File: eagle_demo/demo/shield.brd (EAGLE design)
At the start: 70 x 50 mm, 13 parts, among them X301 MALE_2X1-T-VERTICAL, X302 MALE_2X10-T-VERTICAL_2.54MM

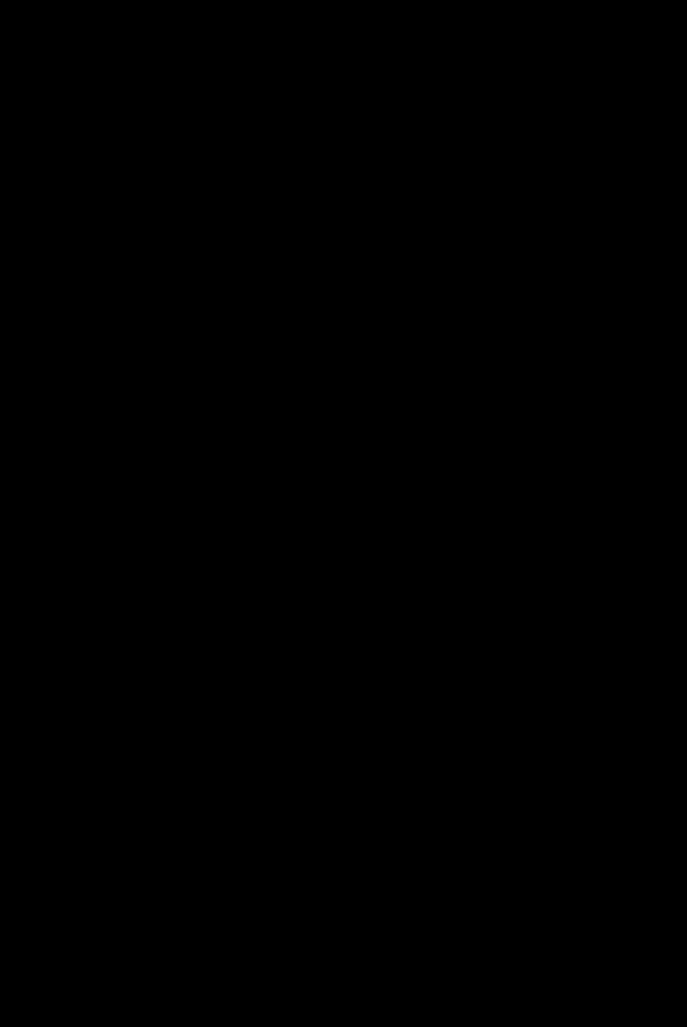
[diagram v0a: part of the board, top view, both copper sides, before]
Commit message: step 1.3 shield schematic updated
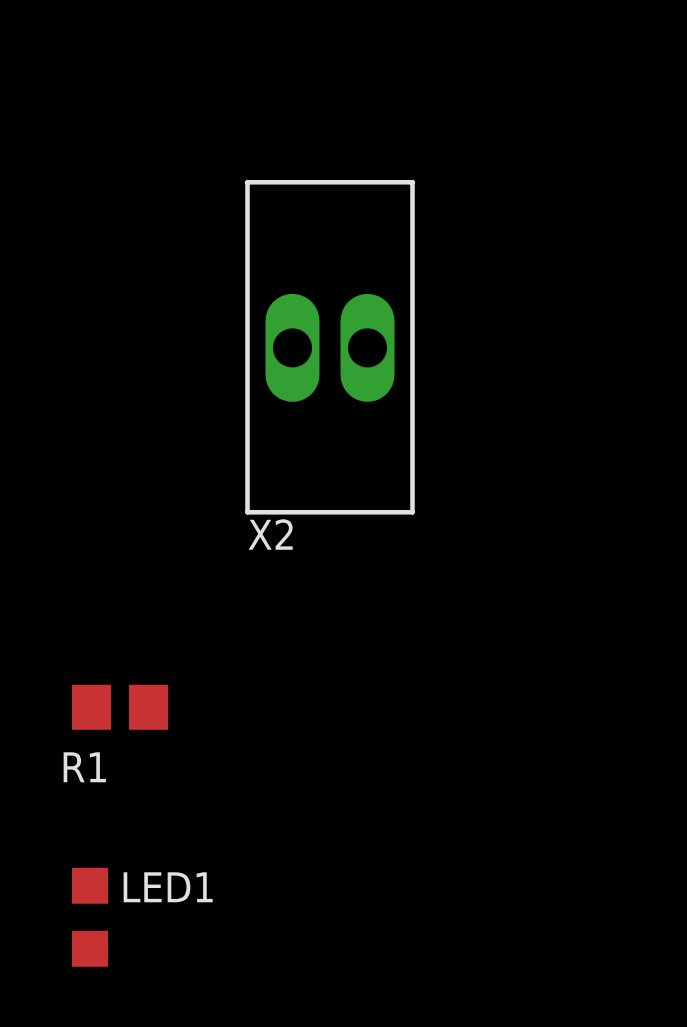
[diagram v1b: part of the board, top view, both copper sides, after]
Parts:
- added LED1: (no value), be_opt:S_0805
- added R1: 330, be_rcl:S_0805
- added X2: CLAMP_1X2-T-2.5MM, be_con_jump:T_WIRE_CLAMP_1X2_PITCH_2MM5
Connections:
- new net KBD_OUT: N2.1, R1.2, X2.2
- new net SH_KBD_DBG: LED1.A, R1.1
- net GND: now also LED1.C, X2.1
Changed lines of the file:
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@@
 <attribute name="VALUE" x="11" y="30" size="1" layer="27" font="vector" ratio="13" rot="R90"/>
+</element>
+<element name="X2" library="be_con_jump" package="T_WIRE_CLAMP_1X2_PITCH_2MM5" value="CLAMP_1X2-T-2.5MM" x="-149" y="-67">
+<attribute name="FUNCTION" value="" x="-149" y="-67" size="1" layer="27" font="vector" ratio="13" display="off"/>
+<attribute name="PART_CODE_EXT" value="" x="-149" y="-67" size="1" layer="27" font="vector" ratio="13" display="off"/>
+<attribute name="PART_CODE_BEL" value="X_PAC_T_CLAMP_1X2_PITCH_2mm5" x="-149" y="-67" size="1" layer="27" font="vector" ratio="13" display="off"/>
+<attribute name="UPDATED" value="" x="-149" y="-67" size="1" layer="27" font="vector" ratio="13" display="off"/>
+<attribute name="BOM" value="YES" x="-149" y="-67" size="1" layer="27" font="vector" ratio="13" display="off"/>
+<attribute name="COMMISSIONED" value="2014-04-14" x="-149" y="-67" size="1" layer="27" font="vector" ratio="13" display="off"/>
+</element>
+<element name="R1" library="be_rcl" package="S_0805" value="330" x="-156" y="-79">
+<attribute name="FUNCTION" value="" x="-164" y="-71" size="1" layer="27" font="vector" ratio="13" display="off"/>
+<attribute name="PART_CODE_EXT" value="" x="-164" y="-71" size="1" layer="27" font="vector" ratio="13" display="off"/>
+<attribute name="PART_CODE_BEL" value="R_PAC_S_0805_VAL_" x="-164" y="-71" size="1" layer="27" font="vector" ratio="13" display="off"/>
+<attribute name="UPDATED" value="" x="-164" y="-71" size="1" layer="27" font="vector" ratio="13" display="off"/>
+<attribute name="BOM" value="YES" x="-164" y="-71" size="1" layer="27" font="vector" ratio="13" display="off"/>
+<attribute name="COMMISSIONED" value="2013-08-30" x="-164" y="-71" size="1" layer="27" font="vector" ratio="13" display="off"/>
+</element>
+<element name="LED1" library="be_opt" package="S_0805" value="" x="-157" y="-86">
+<attribute name="FUNCTION" value="KBD BUTTON PRESSED" x="-164" y="-78" size="1" layer="27" font="vector" ratio="13" display="off"/>
+<attribute name="PART_CODE_EXT" value="" x="-164" y="-78" size="1" layer="27" font="vector" ratio="13" display="off"/>
+<attribute name="PART_CODE_BEL" value="LED_PAC_S_0805_VAL_" x="-164" y="-78" size="1" layer="27" font="vector" ratio="13" display="off"/>
+<attribute name="UPDATED" value="" x="-164" y="-78" size="1" layer="27" font="vector" ratio="13" display="off"/>
+<attribute name="BOM" value="YES" x="-164" y="-78" size="1" layer="27" font="vector" ratio="13" display="off"/>
+<attribute name="COMMISSIONED" value="2013-08-30" x="-164" y="-78" size="1" layer="27" font="vector" ratio="13" display="off"/>
 </element>
 </elements>
@@
 <wire x1="8.95" y1="29" x2="7.8" y2="29" width="0.15" layer="1"/>
 <via x="7.8" y="29" extent="1-16" drill="0.3"/>
+<contactref element="X2" pad="1"/>
+<contactref element="LED1" pad="C"/>
+<wire x1="-150.25" y1="-67.02" x2="-157" y2="-84.95" width="0" layer="19" extent="1-1"/>
+<wire x1="7.8" y1="29" x2="-150.25" y2="-67.02" width="0" layer="19" extent="1-1"/>
+<wire x1="48.73" y1="45" x2="8.95" y2="29" width="0" layer="19" extent="1-1"/>
+<wire x1="61.73" y1="36.43" x2="48.73" y2="45" width="0" layer="19" extent="1-1"/>
+<wire x1="61.73" y1="33.89" x2="61.73" y2="36.43" width="0" layer="19" extent="1-1"/>
 </signal>
 <signal name="MCU_CLK">
@@
 <wire x1="15.05" y1="29" x2="11.05" y2="29" width="0.15" layer="1"/>
 </signal>
+<signal name="KBD_OUT">
+<contactref element="X2" pad="2"/>
+<contactref element="N2" pad="1"/>
+<contactref element="R1" pad="2"/>
+<wire x1="-147.75" y1="-67.02" x2="-155.05" y2="-79" width="0" layer="19" extent="1-1"/>
+<wire x1="55.7" y1="35" x2="-147.75" y2="-67.02" width="0" layer="19" extent="1-1"/>
+</signal>
+<signal name="SH_KBD_DBG">
+<contactref element="R1" pad="1"/>
+<contactref element="LED1" pad="A"/>
+<wire x1="-156.95" y1="-79" x2="-157" y2="-87.05" width="0" layer="19" extent="1-1"/>
+</signal>
 </signals>

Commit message: step 1.5 shield layout
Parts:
- moved X2 216.4 mm to (38.0, 42.0), turned to 180 degrees
- moved R1 205.8 mm to (16.0, 34.0)
- moved LED1 205.6 mm to (10.0, 34.0), turned to 90 degrees
- moved LED4 1.00 mm to (10.0, 28.0)
- moved R4 1.00 mm to (16.0, 28.0)
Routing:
- net KBD_OUT: track 0.00 -> 61.1 mm
- net GND: track 1.15 -> 7.25 mm
- net SH_KBD_DBG: track 0.00 -> 4.00 mm
- net LED_DRV_IN: track 54.9 -> 52.7 mm
